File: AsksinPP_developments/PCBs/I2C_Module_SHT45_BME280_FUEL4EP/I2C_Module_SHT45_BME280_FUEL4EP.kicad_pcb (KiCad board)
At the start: 2 copper layers, 30.5 x 17 mm, 14 parts, among them J1 Conn_01x04, J2 Conn_01x04, U1 BME280, U2 SHT45-AD1F-R2

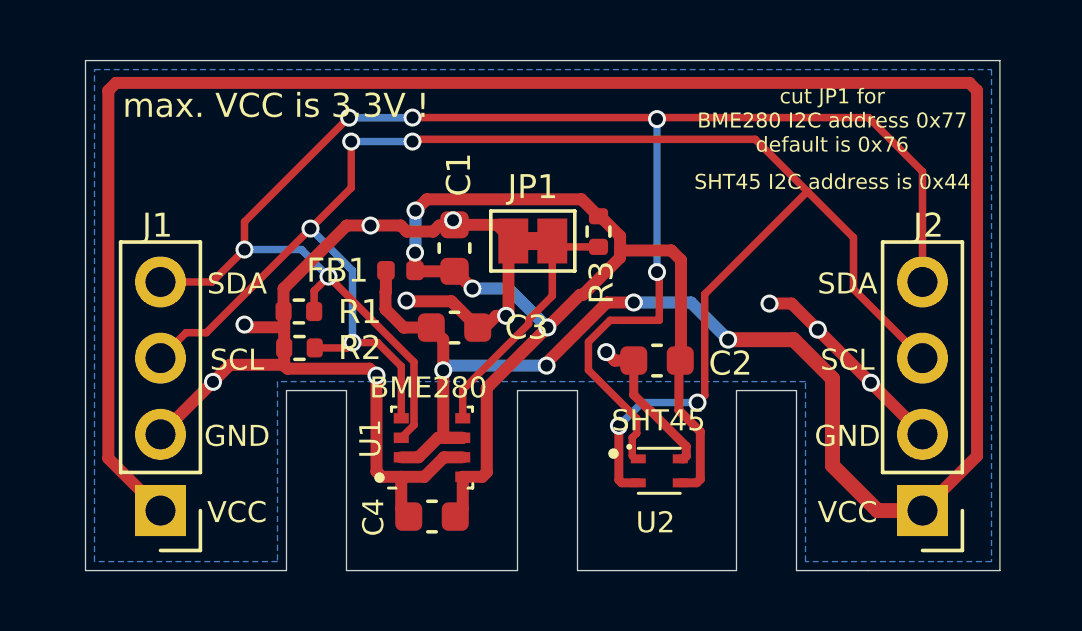
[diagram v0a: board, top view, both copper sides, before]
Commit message: PCBs: HB_TH_Sensor_SHT45_AllInOne_FUEL4EP and I2C_Module_SHT45_BME280_FUEL4EP: replacement of SHT45 to type without PTFE filter
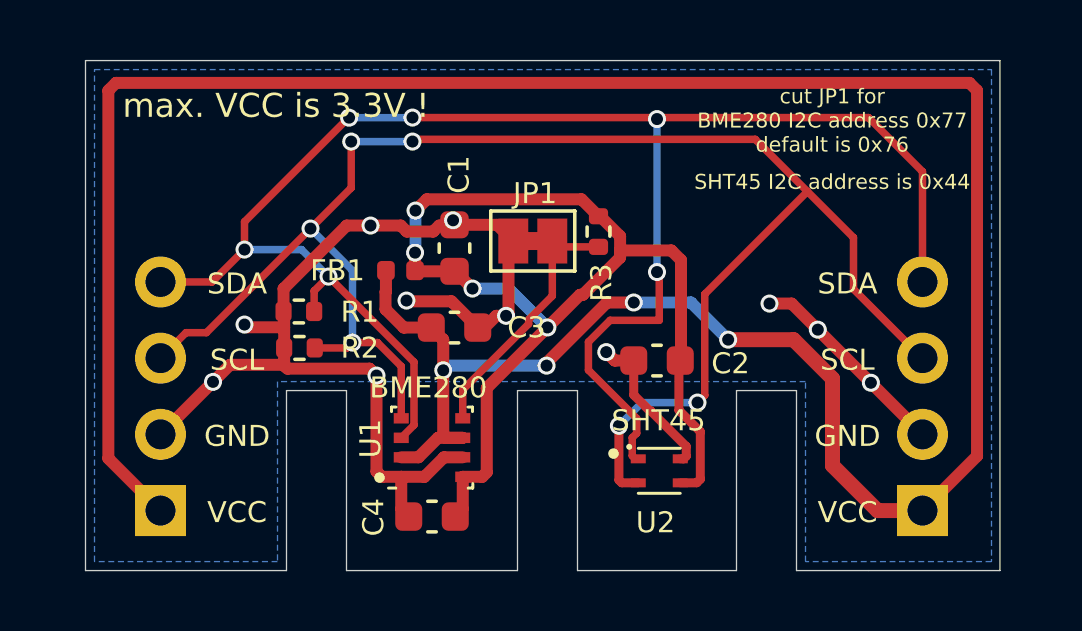
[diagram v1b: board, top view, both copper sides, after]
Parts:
- J1, J2: moved to B.Cu
- U2: value SHT45-AD1F-R2 -> SHT45-AD1B-R2
- turned J1 to 0 degrees
- turned J2 to 0 degrees
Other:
- board text added: "SHT45 BME280 I2C Modul (C) FUEL4EP V1.1 12/2023"
- board text removed: "SHT45 BME280 I2C Modul (C) FUEL4EP V1.0 9/2023"

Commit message: PCBs: fix of I2C Pull-up resistors that were wrongly tied to GND
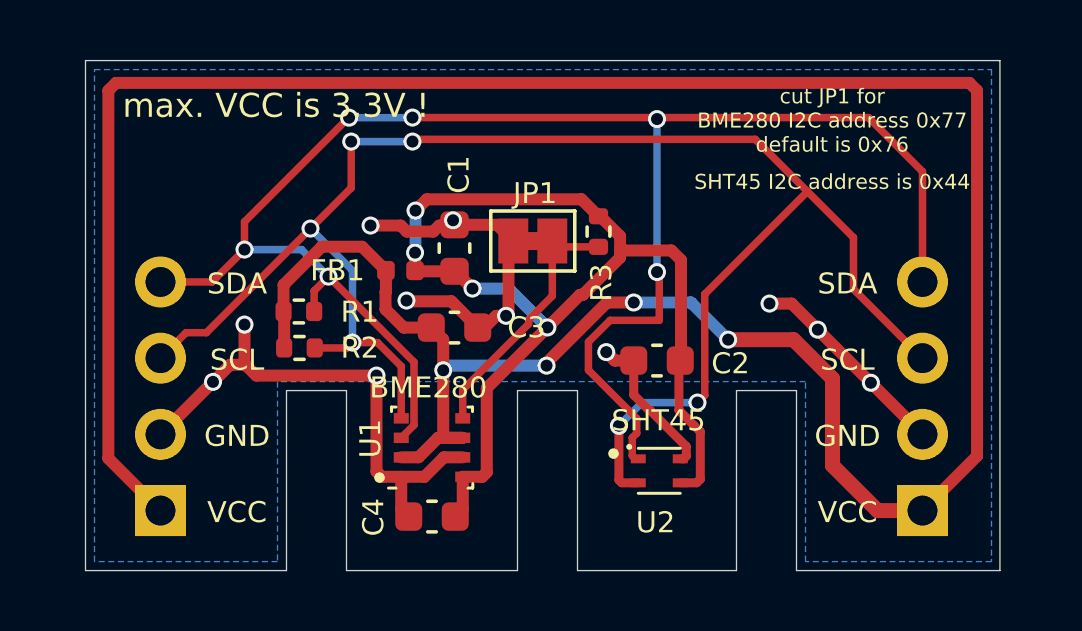
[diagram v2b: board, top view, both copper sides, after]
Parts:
- R1, R2: value 4.7k -> 10k
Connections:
- R1 pad 2: GND -> VCC
- R2 pad 2: GND -> VCC
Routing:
- net GND: track 47.1 -> 40.7 mm
- net VCC: track 90.0 -> 96.4 mm
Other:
- board text added: "SHT45 BME280 I2C Modul (C) FUEL4EP V1.2 02/2024"
- board text removed: "SHT45 BME280 I2C Modul (C) FUEL4EP V1.1 12/2023"
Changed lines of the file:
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@@
   (title_block
     (title "I2C_Module_SHT45_BME280_FUEL4EP")
-    (date "2023-12-15")
-    (rev "V1.1")
+    (date "2024-02-08")
+    (rev "V1.2")
     (company "(c) FUEL4EP")
   )
@@
     (descr "Resistor SMD 0402 (1005 Metric), square (rectangular) end terminal, IPC_7351 nominal, (Body size source: IPC-SM-782 page 72, https://www.pcb-3d.com/wordpress/wp-content/uploads/ipc-sm-782a_amendment_1_and_2.pdf), generated with kicad-footprint-generator")
     (tags "resistor")
-    (property "LCSC" "C25900")
+    (property "LCSC" "C25744")
     (property "Sheetfile" "I2C_Module_SHT45_BME280_FUEL4EP.kicad_sch")
     (property "Sheetname" "")
@@
       (effects (font (size 0.7 0.7) (thickness 0.15)))
     )
-    (fp_text value "4.7k" (at -0.12 -0.015) (layer "F.Fab")
+    (fp_text value "10k" (at -0.12 -0.015) (layer "F.Fab")
       (effects (font (size 0.7 0.7) (thickness 0.15)))
     )
@@
       (net 4 "/SDA") (pintype "passive"))
     (pad "2" smd roundrect (at 0.51 0 180) (size 0.54 0.64) (layers "F.Cu" "F.Paste" "F.Mask") (roundrect_rratio 0.25)
-      (net 2 "GND") (pintype "passive"))
+      (net 1 "VCC") (pintype "passive"))
     (model "${KICAD6_3DMODEL_DIR}/Resistor_SMD.3dshapes/R_0402_1005Metric.wrl"
       (offset (xyz 0 0 0))
@@
     (descr "Resistor SMD 0402 (1005 Metric), square (rectangular) end terminal, IPC_7351 nominal, (Body size source: IPC-SM-782 page 72, https://www.pcb-3d.com/wordpress/wp-content/uploads/ipc-sm-782a_amendment_1_and_2.pdf), generated with kicad-footprint-generator")
     (tags "resistor")
-    (property "LCSC" "C25900")
+    (property "LCSC" "C25744")
     (property "Sheetfile" "I2C_Module_SHT45_BME280_FUEL4EP.kicad_sch")
     (property "Sheetname" "")
@@
       (effects (font (size 0.7 0.7) (thickness 0.15)))
     )
-    (fp_text value "4.7k" (at -0.2 -0.1) (layer "F.Fab")
+    (fp_text value "10k" (at -0.2 -0.1) (layer "F.Fab")
       (effects (font (size 0.7 0.7) (thickness 0.15)))
     )
@@
       (net 3 "/SCL") (pintype "passive"))
     (pad "2" smd roundrect (at 0.51 0 180) (size 0.54 0.64) (layers "F.Cu" "F.Paste" "F.Mask") (roundrect_rratio 0.25)
-      (net 2 "GND") (pintype "passive"))
+      (net 1 "VCC") (pintype "passive"))
     (model "${KICAD6_3DMODEL_DIR}/Resistor_SMD.3dshapes/R_0402_1005Metric.wrl"
       (offset (xyz 0 0 0))
@@
   (gr_line (start 21.7 0) (end 16.4 0) (layer "Edge.Cuts") (width 0.0381))
   (gr_line (start 30.48 -17) (end 30.48 0) (layer "Edge.Cuts") (width 0.0381))
-  (gr_text "SHT45 BME280\nI2C Modul\n(C) FUEL4EP\nV1.1\n12/2023" (at 15.748 -9.144) (layer "B.SilkS")
+  (gr_text "SHT45 BME280\nI2C Modul\n(C) FUEL4EP\nV1.2\n02/2024" (at 15.748 -9.144) (layer "B.SilkS")
     (effects (font (size 0.7 0.7) (thickness 0.1524)) (justify mirror))
   )
@@
   (segment (start 26.4 -2) (end 24.9 -3.5) (width 0.5) (layer "F.Cu") (net 1))
   (segment (start 11.75 -4.425) (end 11.1 -3.775) (width 0.4) (layer "F.Cu") (net 1))
+  (segment (start 7.874 -10.795) (end 9.22 -10.795) (width 0.4) (layer "F.Cu") (net 1))
   (segment (start 17.380493 -8.935823) (end 18.274735 -8.935823) (width 0.4) (layer "F.Cu") (net 1))
   (segment (start 1.016 -16.256) (end 29.464 -16.256) (width 0.4) (layer "F.Cu") (net 1))
+  (segment (start 6.602 -9.523) (end 7.874 -10.795) (width 0.4) (layer "F.Cu") (net 1))
   (segment (start 11.1 -3.775) (end 10.525 -3.775) (width 0.4) (layer "F.Cu") (net 1))
   (segment (start 15.368742 -6.924072) (end 17.380493 -8.935823) (width 0.4) (layer "F.Cu") (net 1))
@@
   (segment (start 29.464 -16.256) (end 29.718 -16.002) (width 0.4) (layer "F.Cu") (net 1))
   (segment (start 0.762 -3.738) (end 0.762 -16.002) (width 0.4) (layer "F.Cu") (net 1))
+  (segment (start 6.622 -8.616) (end 6.602 -8.636) (width 0.4) (layer "F.Cu") (net 1))
   (segment (start 10.0005 -8.710257) (end 10.610757 -8.1) (width 0.4) (layer "F.Cu") (net 1))
+  (segment (start 6.602 -8.636) (end 6.602 -9.523) (width 0.4) (layer "F.Cu") (net 1))
   (segment (start 10.0005 -9.289743) (end 10.0005 -8.710257) (width 0.4) (layer "F.Cu") (net 1))
   (segment (start 10.015 -10) (end 10.015 -9.304243) (width 0.4) (layer "F.Cu") (net 1))
   (segment (start 11.925 -4.5) (end 11.925 -7.7) (width 0.4) (layer "F.Cu") (net 1))
+  (segment (start 9.22 -10.795) (end 10.015 -10) (width 0.4) (layer "F.Cu") (net 1))
   (segment (start 0.762 -16.002) (end 1.016 -16.256) (width 0.4) (layer "F.Cu") (net 1))
   (segment (start 10.610757 -8.1) (end 11.525 -8.1) (width 0.4) (layer "F.Cu") (net 1))
@@
   (segment (start 24.9 -3.5) (end 24.9 -6.4) (width 0.5) (layer "F.Cu") (net 1))
   (segment (start 12.575 -4.425) (end 11.75 -4.425) (width 0.4) (layer "F.Cu") (net 1))
+  (segment (start 6.622 -7.421) (end 6.622 -8.616) (width 0.4) (layer "F.Cu") (net 1))
   (segment (start 0.762 -3.738) (end 2.5 -2) (width 0.4) (layer "F.Cu") (net 1))
   (segment (start 11.925 -7.7) (end 11.525 -8.1) (width 0.4) (layer "F.Cu") (net 1))
@@
   (segment (start 14.1 -8.572728) (end 14.019014 -8.491742) (width 0.4) (layer "F.Cu") (net 2))
   (segment (start 9.7 -3.3) (end 9.7 -6.5) (width 0.4) (layer "F.Cu") (net 2))
-  (segment (start 6.602 -9.396) (end 6.602 -8.636) (width 0.4) (layer "F.Cu") (net 2))
   (segment (start 18.796 -5.334) (end 18.275 -5.855) (width 0.3) (layer "F.Cu") (net 2))
+  (segment (start 4.818 -6.858) (end 5.334 -6.858) (width 0.4) (layer "F.Cu") (net 2))
+  (segment (start 9.7 -6.5) (end 5.692 -6.5) (width 0.4) (layer "F.Cu") (net 2))
   (segment (start 10.725 -8.975) (end 10.7 -9) (width 0.4) (layer "F.Cu") (net 2))
-  (segment (start 9.469 -6.731) (end 9.7 -6.5) (width 0.4) (layer "F.Cu") (net 2))
   (segment (start 10.510257 -11.5005) (end 9.5005 -11.5005) (width 0.4) (layer "F.Cu") (net 2))
   (segment (start 18.828132 -5.334) (end 20.025 -4.137132) (width 0.3) (layer "F.Cu") (net 2))
   (segment (start 14.1 -10.825) (end 14.1 -8.572728) (width 0.4) (layer "F.Cu") (net 2))
+  (segment (start 5.3 -8.2) (end 5.3 -6.892) (width 0.4) (layer "F.Cu") (net 2))
   (segment (start 13.691742 -8.491742) (end 14.019014 -8.491742) (width 0.4) (layer "F.Cu") (net 2))
   (segment (start 24.41 -8.03) (end 23.54 -8.9) (width 0.4) (layer "F.Cu") (net 2))
   (segment (start 18.275 -5.855) (end 18.275 -7) (width 0.3) (layer "F.Cu") (net 2))
-  (segment (start 6.622 -8.11) (end 5.39 -8.11) (width 0.4) (layer "F.Cu") (net 2))
   (segment (start 11.589743 -11.3005) (end 10.710257 -11.3005) (width 0.4) (layer "F.Cu") (net 2))
   (segment (start 10.525 -3.125) (end 10.525 -2.05) (width 0.4) (layer "F.Cu") (net 2))
   (segment (start 17.641051 -7) (end 17.3585 -7.282551) (width 0.4) (layer "F.Cu") (net 2))
   (segment (start 20.025 -3.812868) (end 19.937132 -3.725) (width 0.3) (layer "F.Cu") (net 2))
-  (segment (start 6.731 -6.731) (end 9.469 -6.731) (width 0.4) (layer "F.Cu") (net 2))
   (segment (start 13.3 -8.1) (end 13.691742 -8.491742) (width 0.4) (layer "F.Cu") (net 2))
-  (segment (start 6.682 -6.78) (end 6.731 -6.731) (width 0.4) (layer "F.Cu") (net 2))
   (segment (start 12.2755 -11.5005) (end 11.789743 -11.5005) (width 0.4) (layer "F.Cu") (net 2))
   (segment (start 20.025 -4.137132) (end 20.025 -3.812868) (width 0.3) (layer "F.Cu") (net 2))
-  (segment (start 5.39 -8.11) (end 5.3 -8.2) (width 0.4) (layer "F.Cu") (net 2))
-  (segment (start 6.622 -6.84) (end 6.682 -6.78) (width 0.4) (layer "F.Cu") (net 2))
   (segment (start 26.18 -6.26) (end 24.41 -8.03) (width 0.4) (layer "F.Cu") (net 2))
   (segment (start 23.54 -8.9) (end 22.8 -8.9) (width 0.4) (layer "F.Cu") (net 2))
   (segment (start 13.075 -8.1) (end 12.2 -8.975) (width 0.4) (layer "F.Cu") (net 2))
-  (segment (start 4.818 -6.858) (end 6.604 -6.858) (width 0.4) (layer "F.Cu") (net 2))
   (segment (start 18.828132 -5.334) (end 18.796 -5.334) (width 0.3) (layer "F.Cu") (net 2))
+  (segment (start 5.692 -6.5) (end 5.334 -6.858) (width 0.4) (layer "F.Cu") (net 2))
   (segment (start 11.789743 -11.5005) (end 11.589743 -11.3005) (width 0.4) (layer "F.Cu") (net 2))
+  (segment (start 5.3 -6.892) (end 5.334 -6.858) (width 0.4) (layer "F.Cu") (net 2))
   (segment (start 12.575 -3.775) (end 11.947822 -3.775) (width 0.4) (layer "F.Cu") (net 2))
-  (segment (start 6.622 -7.421) (end 6.622 -6.84) (width 0.4) (layer "F.Cu") (net 2))
   (segment (start 13.72 -11.525) (end 14.26 -10.985) (width 0.4) (layer "F.Cu") (net 2))
   (segment (start 10.525 -3.125) (end 9.875 -3.125) (width 0.4) (layer "F.Cu") (net 2))
   (segment (start 12.3 -11.525) (end 13.72 -11.525) (width 0.4) (layer "F.Cu") (net 2))
-  (segment (start 6.622 -8.11) (end 6.622 -8.616) (width 0.4) (layer "F.Cu") (net 2))
-  (segment (start 6.604 -6.858) (end 6.682 -6.78) (width 0.4) (layer "F.Cu") (net 2))
   (segment (start 11.297822 -3.125) (end 10.525 -3.125) (width 0.4) (layer "F.Cu") (net 2))
   (segment (start 11.947822 -3.775) (end 11.297822 -3.125) (width 0.4) (layer "F.Cu") (net 2))
   (segment (start 10.710257 -11.3005) (end 10.510257 -11.5005) (width 0.4) (layer "F.Cu") (net 2))
   (segment (start 2.5 -4.54) (end 4.25 -6.29) (width 0.4) (layer "F.Cu") (net 2))
-  (segment (start 8.7065 -11.5005) (end 6.602 -9.396) (width 0.4) (layer "F.Cu") (net 2))
-  (segment (start 9.5005 -11.5005) (end 8.7065 -11.5005) (width 0.4) (layer "F.Cu") (net 2))
   (segment (start 27.9 -4.54) (end 26.18 -6.26) (width 0.4) (layer "F.Cu") (net 2))
-  (segment (start 6.622 -7.421) (end 6.622 -8.11) (width 0.4) (layer "F.Cu") (net 2))
   (segment (start 4.25 -6.29) (end 4.818 -6.858) (width 0.4) (layer "F.Cu") (net 2))
   (via (at 4.25 -6.29) (size 0.6) (drill 0.4) (layers "F.Cu" "B.Cu") (net 2))

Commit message: PCBs: upgrade some PCBs to KiCAD 7; fix of unnecessary leakage current of I2C address selector: I2C_Module_SHT85_BME280_FUEL4EP, I2C_Module_SHT45_BME280_small_FUEL4EP, I2C_Module_SHT45_BME280_FUEL4EP, I2C_Module_BME280_FUEL4EP, and I2C_Module_BME680_FUEL4EP
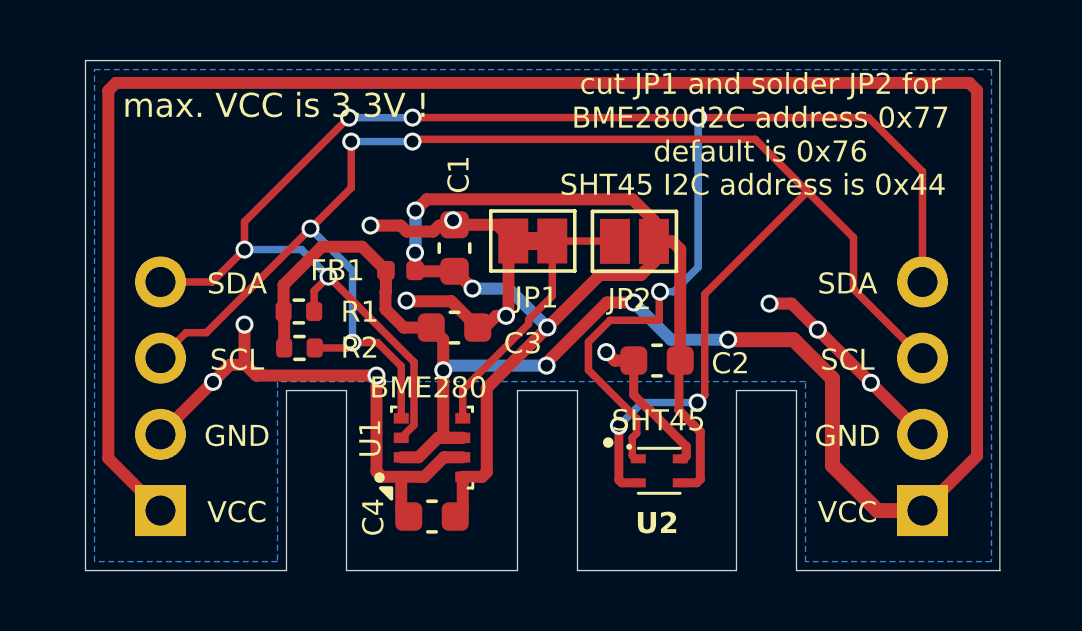
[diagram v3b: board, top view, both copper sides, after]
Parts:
- removed R3: 10k, Resistor_SMD:R_0402_1005Metric
- added JP2: SolderJumper_2_Open, Jumper:SolderJumper-2_P1.3mm_Open_Pad1.0x1.5mm, F.Cu at (18.3, -11.0)
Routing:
- net VDDA: track 37.1 -> 39.0 mm
- net Net-(JP1-B): track 8.49 -> 9.95 mm
- net /SDA: track 58.0 -> 58.8 mm
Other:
- board text added: "SHT45 BME280 I2C Modul (C) FUEL4EP V1.3 04/2024"
- board text added: "cut JP1 and solder JP2 for BME280 I2C address 0x77 default is 0x76"
- board text removed: "SHT45 BME280 I2C Modul (C) FUEL4EP V1.2 02/2024"
- board text removed: "cut JP1 for BME280 I2C address 0x77 default is 0x76"

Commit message: PCBs/I2C_Module_SHT45_BME280_FUEL4EP und PCBs/I2C_Module_BME280_FUEL4EP: migration to KiCAD 8; fix of DRC rules for PCBs/I2C_Module_SHT45_BME280_FUEL4EP
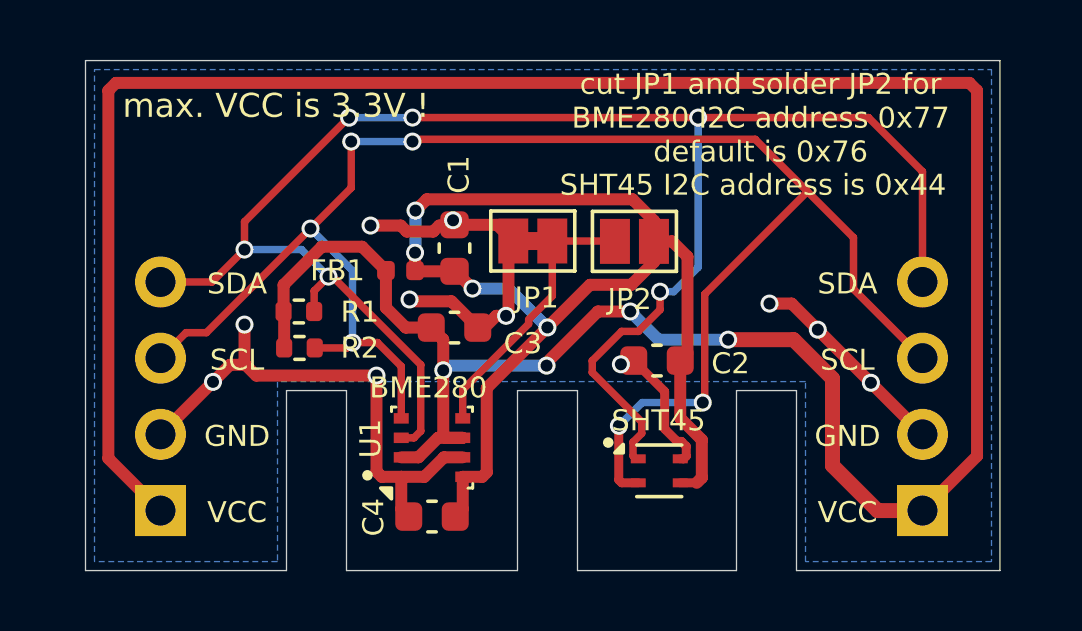
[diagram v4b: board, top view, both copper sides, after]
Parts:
- U2: footprint FUEL4EP:SHT4X -> Sensor_Humidity:Sensirion_DFN-4_1.5x1.5mm_P0.8mm_SHT4x_NoCentralPad
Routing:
- net Net-(JP1-B): track 9.95 -> 9.22 mm
- net GND: track 40.7 -> 40.2 mm
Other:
- board text added: "SHT45 BME280 I2C Modul (C) FUEL4EP V1.4 09/2024"
- board text removed: "SHT45 BME280 I2C Modul (C) FUEL4EP V1.3 04/2024"

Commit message: PCBs/I2C_Module_SHT45_BME280_FUEL4EP: added additional VCC wire
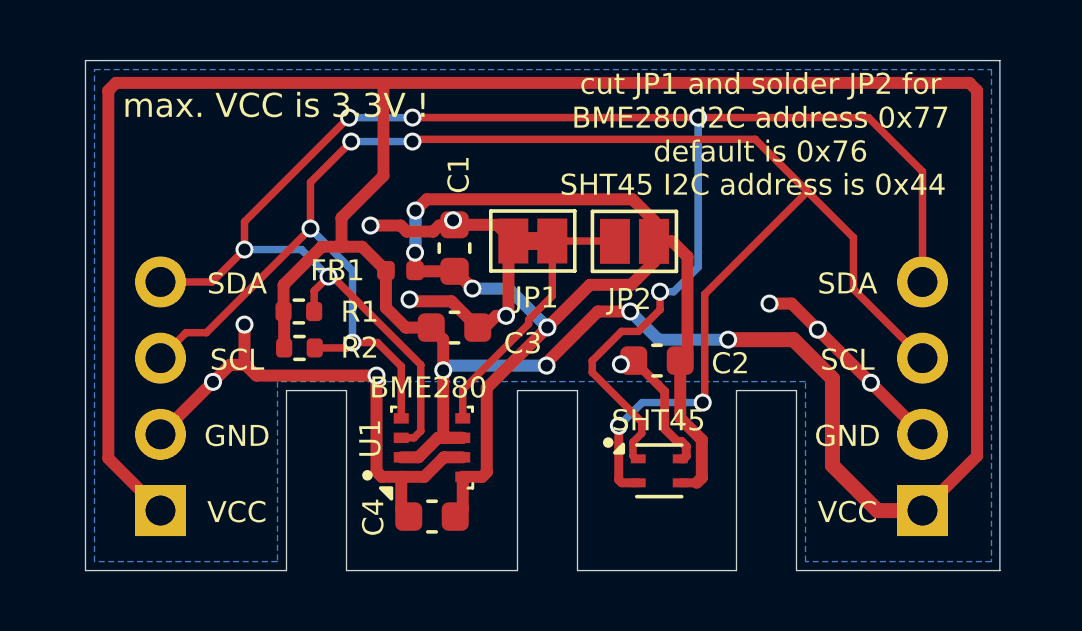
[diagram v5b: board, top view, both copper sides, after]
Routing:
- net VCC: track 96.1 -> 102.1 mm
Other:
- board text added: "SHT45 BME280 I2C Modul (C) FUEL4EP V1.5 10/2024"
- board text removed: "SHT45 BME280 I2C Modul (C) FUEL4EP V1.4 09/2024"
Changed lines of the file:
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@@
 	(title_block
 		(title "I2C_Module_SHT45_BME280_FUEL4EP")
-		(date "2024-09-30")
-		(rev "V1.4")
+		(date "2024-10-02")
+		(rev "V1.5")
 		(company "(c) FUEL4EP")
 	)
@@
 		(layer "Edge.Cuts")
 	)
-	(gr_text "SHT45 BME280\nI2C Modul\n(C) FUEL4EP\nV1.4\n09/2024"
+	(gr_text "SHT45 BME280\nI2C Modul\n(C) FUEL4EP\nV1.5\n10/2024"
 		(at 15.748 -9.144 0)
 		(layer "B.SilkS")
@@
 	)
 	(segment
-		(start 7.874 -10.795)
-		(end 9.22 -10.795)
-		(width 0.4)
-		(layer "F.Cu")
-		(net 1)
-	)
-	(segment
-		(start 1.016 -16.256)
-		(end 29.464 -16.256)
+		(start 9.9314 -13.1572)
+		(end 8.5344 -11.7602)
 		(width 0.4)
 		(layer "F.Cu")
@@
 	)
 	(segment
+		(start 8.5344 -10.795)
+		(end 9.22 -10.795)
+		(width 0.4)
+		(layer "F.Cu")
+		(net 1)
+	)
+	(segment
 		(start 6.602 -8.636)
 		(end 6.602 -9.523)
@@
 	)
 	(segment
+		(start 9.9314 -16.256)
+		(end 29.464 -16.256)
+		(width 0.4)
+		(layer "F.Cu")
+		(net 1)
+	)
+	(segment
 		(start 10.015 -10)
 		(end 10.015 -8.761462)
@@
 	)
 	(segment
+		(start 7.874 -10.795)
+		(end 8.5344 -10.795)
+		(width 0.4)
+		(layer "F.Cu")
+		(net 1)
+	)
+	(segment
 		(start 24.9 -3.5)
 		(end 24.9 -6.4)
@@
 	)
 	(segment
+		(start 9.9314 -16.256)
+		(end 9.9314 -13.1572)
+		(width 0.4)
+		(layer "F.Cu")
+		(net 1)
+	)
+	(segment
 		(start 29.718 -16.002)
 		(end 29.718 -3.818)
@@
 		(net 1)
 	)
+	(segment
+		(start 8.5344 -11.7602)
+		(end 8.5344 -10.795)
+		(width 0.4)
+		(layer "F.Cu")
+		(net 1)
+	)
+	(segment
+		(start 1.016 -16.256)
+		(end 9.9314 -16.256)
+		(width 0.4)
+		(layer "F.Cu")
+		(net 1)
+	)
 	(via
 		(at 18.160998 -8.636)
@@
 	)
 	(segment
-		(start 7.5 -11.4)
-		(end 8.857217 -12.757217)
-		(width 0.25)
-		(layer "F.Cu")
-		(net 3)
-	)
-	(segment
 		(start 2.5 -7.08)
 		(end 3.35 -7.93)
@@
 	)
 	(segment
-		(start 8.857217 -12.757217)
-		(end 8.857217 -14.3)
+		(start 10.9 -14.3)
+		(end 10.9745 -14.3745)
 		(width 0.25)
 		(layer "F.Cu")
@@
 	)
 	(segment
-		(start 10.9 -14.3)
-		(end 10.9745 -14.3745)
+		(start 7.5 -12.942783)
+		(end 8.857217 -14.3)
 		(width 0.25)
 		(layer "F.Cu")
@@
 		(layer "F.Cu")
 		(net 3)
+	)
+	(segment
+		(start 7.5 -11.4)
+		(end 7.5 -12.942783)
+		(width 0.25)
+		(layer "F.Cu")
+		(net 3)
